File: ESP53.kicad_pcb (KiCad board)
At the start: 4 copper layers, 19.2 x 25 mm, 58 parts, among them IC1 ESP32-C5HR8, J2 Conn_02x04_Odd_Even, J3 USB_C_Receptacle_USB2.0_16P, SW1 SW_Push, SW2 SW_Push, U2 LN1134A332MR, Y1 48MHz

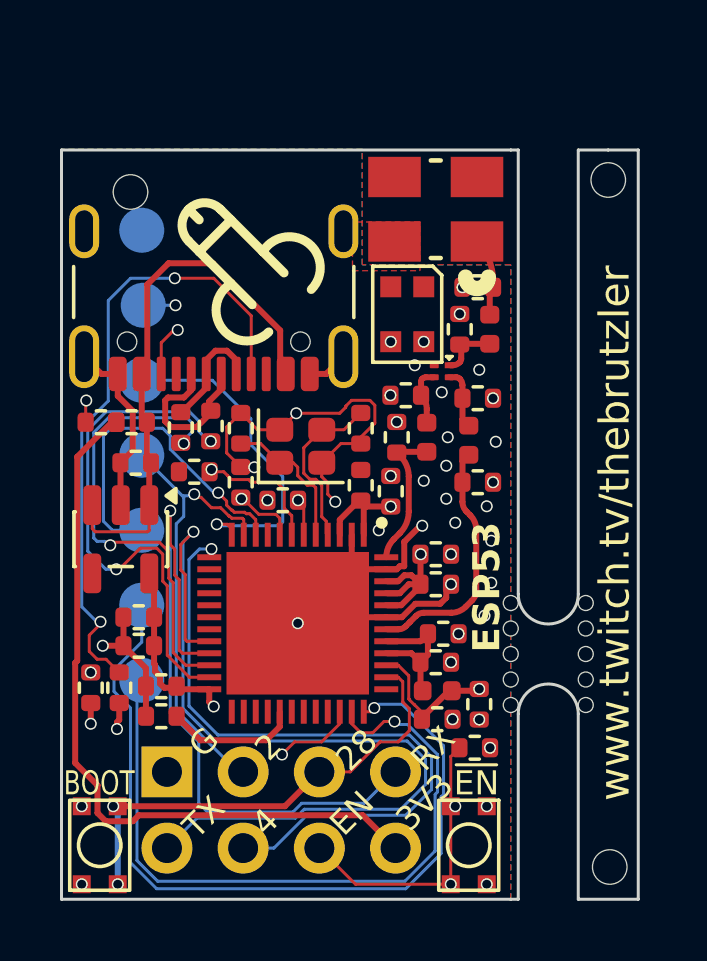
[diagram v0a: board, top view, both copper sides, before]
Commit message: update wifi connection routing
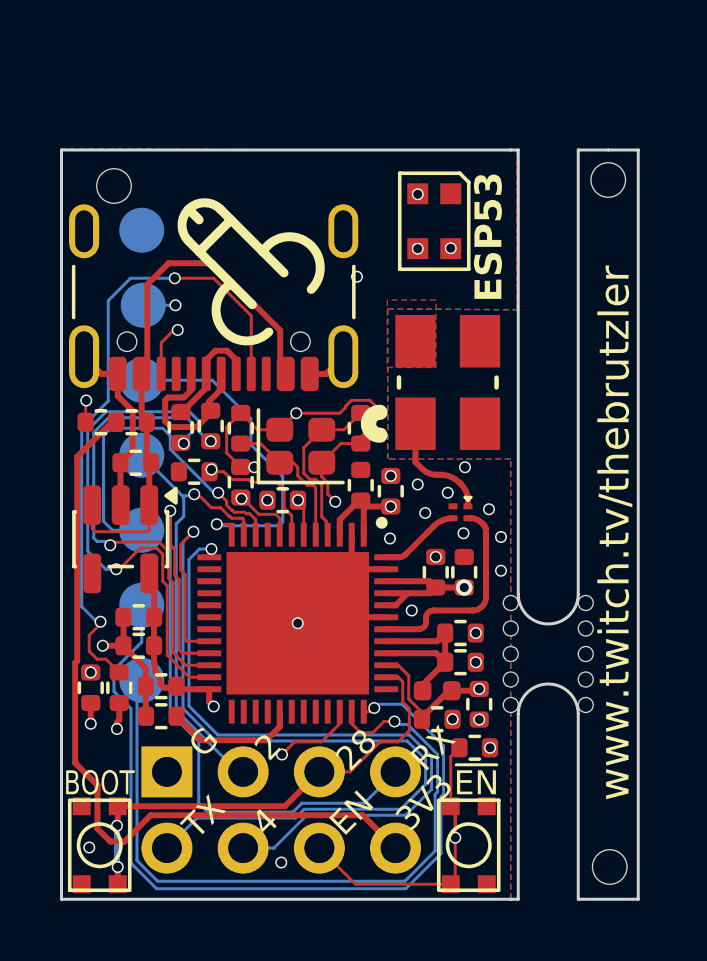
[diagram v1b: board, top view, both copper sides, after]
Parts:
- removed C25, C26, C27, C28, C29, C30: 9p, Resistor_SMD:R_0402_1005Metric
- removed L4, L5, L6: 2n2, Inductor_SMD:L_0402_1005Metric
- moved AE2 5.79 mm to (155.1, 104.7), turned to 180 degrees
- moved U3 4.74 mm to (155.5, 109.0)
- moved D1 3.23 mm to (154.7, 99.3)
- moved C13 1.12 mm to (155.7, 111.0), turned to 90 degrees
- moved C20 0.83 mm to (155.5, 114.0)
- moved REF** 0.59 mm to (144.0, 98.1)
- moved C19 0.58 mm to (155.5, 113.0)
- moved C22 0.40 mm to (154.7, 111.0), turned to 90 degrees
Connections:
- U3 pad 1: Net-(U3-COM) -> Net-(AE2-A)
- U3 pad 3: Net-(U3-HB) -> Net-(IC1-ANT_5G)
- U3 pad 4: Net-(U3-LB) -> Net-(IC1-ANT_2G)
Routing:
- net GND: track 38.7 -> 33.6 mm, vias 39 -> 28
- net Net-(IC1-ANT_5G): track 4.84 -> 2.71 mm
- net Net-(U3-LB): track 2.04 -> 0.00 mm
- net /EN: track 32.3 -> 34.3 mm, vias 3 -> 2
- net Net-(U3-COM): track 2.00 -> 0.00 mm
- net Net-(U3-HB): track 1.94 -> 0.00 mm
- net /RADIO_VDD: track 4.82 -> 6.50 mm
- net Net-(IC1-ANT_2G): track 8.30 -> 6.97 mm
- net /IO24: track 26.1 -> 27.4 mm
- net Net-(AE2-A): track 2.60 -> 3.82 mm
- net Net-(J2-Pin_8): track 24.6 -> 25.4 mm
- net +3V3: track 25.0 -> 25.3 mm, vias 11 -> 10
